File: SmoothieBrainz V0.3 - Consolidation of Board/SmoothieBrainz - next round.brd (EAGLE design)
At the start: 101 x 101 mm, 222 parts, among them IC1 LPC1769, IC5 LD117ADT33TR, Q1 BSL207SP, Q2 12MHz, SW1 SW_TACT_4P_B, SW3 SW_TACT_4P_B, T1 BC817, U3 USD-SOCKETUSD, X1 MSTBA2, X14 USBPTH, X2 GMSTBA2, X3 GMSTBA4, X4 1751248, X5 1751248, X6 1751248, X7 1751248

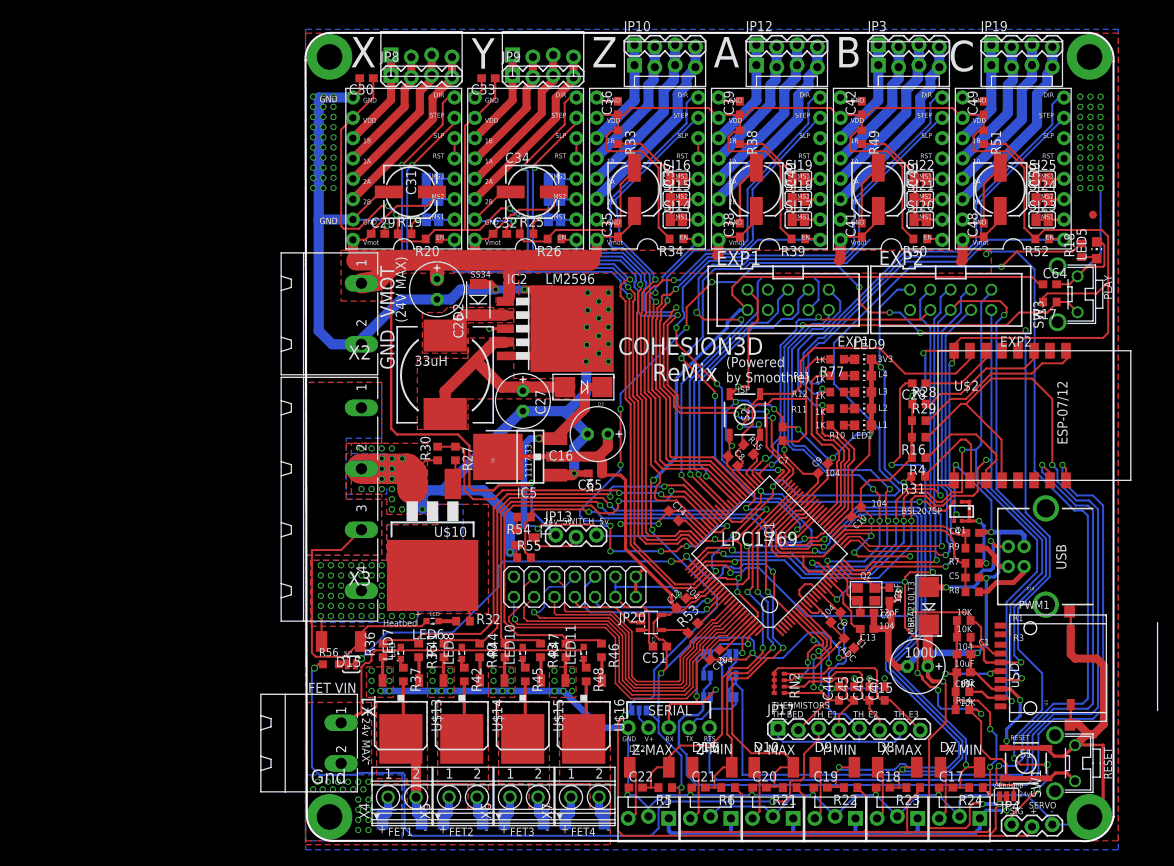
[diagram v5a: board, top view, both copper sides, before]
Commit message: motor 3 re-routed
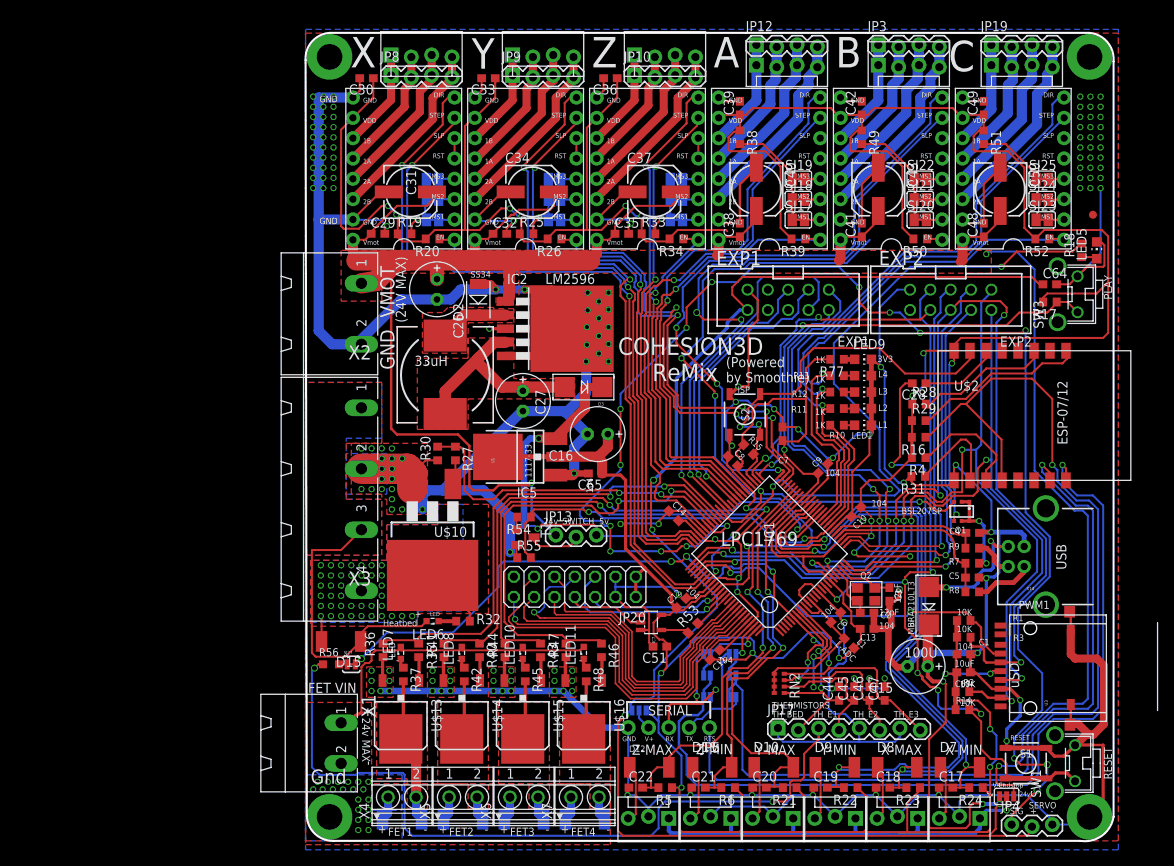
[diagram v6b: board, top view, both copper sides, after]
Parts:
- moved R33 12.7 mm to (42.9, 75.9), turned to 0 degrees
- moved C36 3.85 mm to (38.1, 95.3), turned to 180 degrees
- moved JP10 3.81 mm to (41.1, 95.6)
- moved C37 2.48 mm to (43.6, 81.1), turned to 0 degrees
- moved JP7 1.27 mm to (41.1, 98.1)
- moved C35 0.67 mm to (39.5, 75.9), turned to 0 degrees
- flipped SJ14 to the bottom, turned to 180 degrees
- flipped SJ15 to the bottom, turned to 180 degrees
- flipped SJ16 to the bottom, turned to 180 degrees
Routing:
- net 24V: track 256.6 -> 263.3 mm
- net N$24: track 13.9 -> 8.45 mm, vias 0 -> 1
- net DIR3: track 65.9 -> 61.5 mm, vias 1 -> 2
- net STP3: track 66.4 -> 62.5 mm, vias 1 -> 2
- net 3.3V: track 684.9 -> 687.1 mm, vias 23 -> 25
- net 2A3M: track 20.8 -> 19.5 mm
- net 1B3M: track 13.6 -> 12.4 mm
- net 1A3M: track 17.0 -> 15.7 mm
- net 2B3M: track 24.1 -> 22.9 mm
- net GND: track 776.5 -> 777.5 mm, vias 162 -> 163

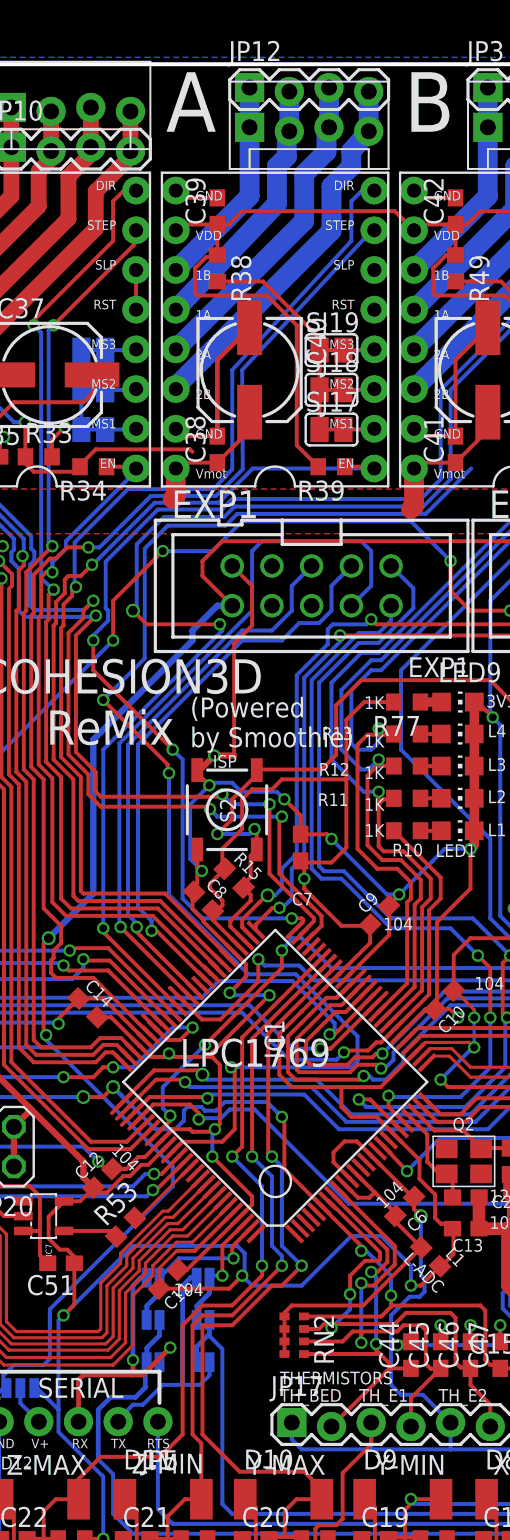
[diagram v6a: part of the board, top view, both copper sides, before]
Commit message: motor 4 wires
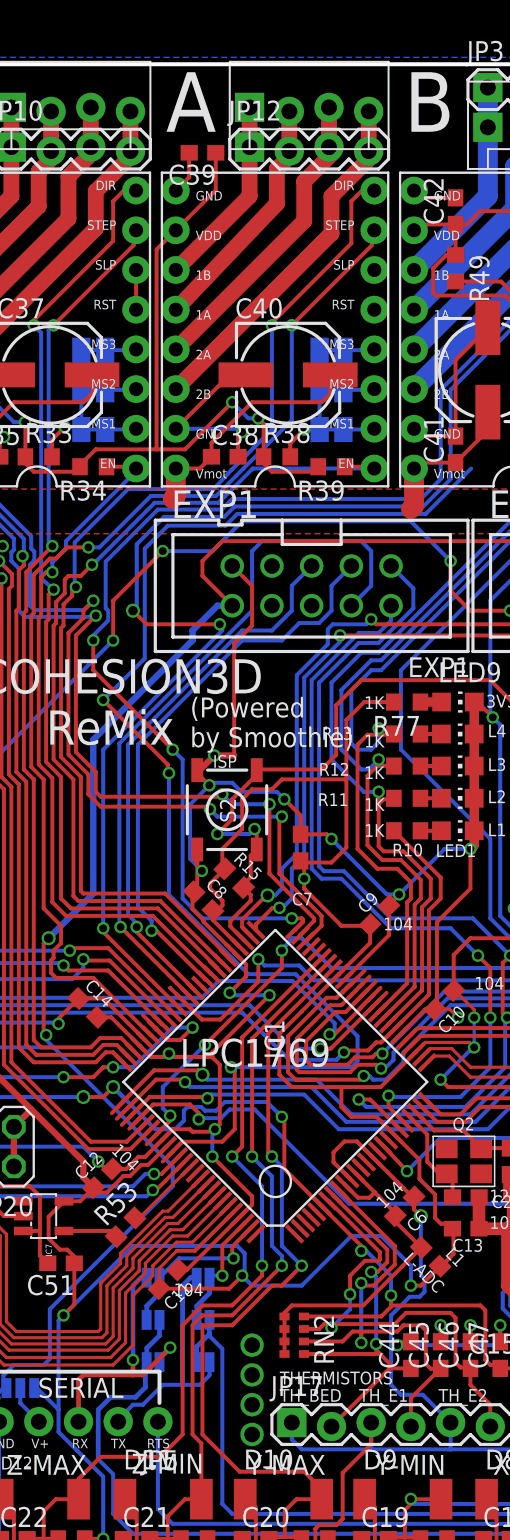
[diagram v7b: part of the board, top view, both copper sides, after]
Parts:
- moved R38 12.7 mm to (58.1, 75.9), turned to 0 degrees
- moved C39 3.85 mm to (53.3, 95.3), turned to 180 degrees
- moved JP12 3.81 mm to (56.4, 95.6)
- moved C40 2.48 mm to (58.8, 81.1), turned to 0 degrees
- moved JP11 1.27 mm to (56.4, 98.1)
- moved C38 0.67 mm to (54.8, 75.9), turned to 0 degrees
- flipped SJ17 to the bottom, turned to 180 degrees
- flipped SJ18 to the bottom, turned to 180 degrees
- flipped SJ19 to the bottom, turned to 180 degrees
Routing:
- net 24V: track 263.3 -> 269.7 mm
- net N$32: track 14.0 -> 8.41 mm, vias 0 -> 1
- net 3.3V: track 687.1 -> 682.4 mm, vias 25 -> 27
- net 1B$4M: track 13.6 -> 12.4 mm
- net 2B$4M: track 24.1 -> 22.9 mm
- net 2A$4M: track 20.8 -> 19.7 mm
- net 1A$4M: track 16.9 -> 15.7 mm
- net GND: track 777.5 -> 778.4 mm, vias 163 -> 164
- net STP4: track 69.5 -> 69.8 mm, vias 1 -> 2
- net DIR4: track 68.4 -> 68.6 mm, vias 1 -> 2

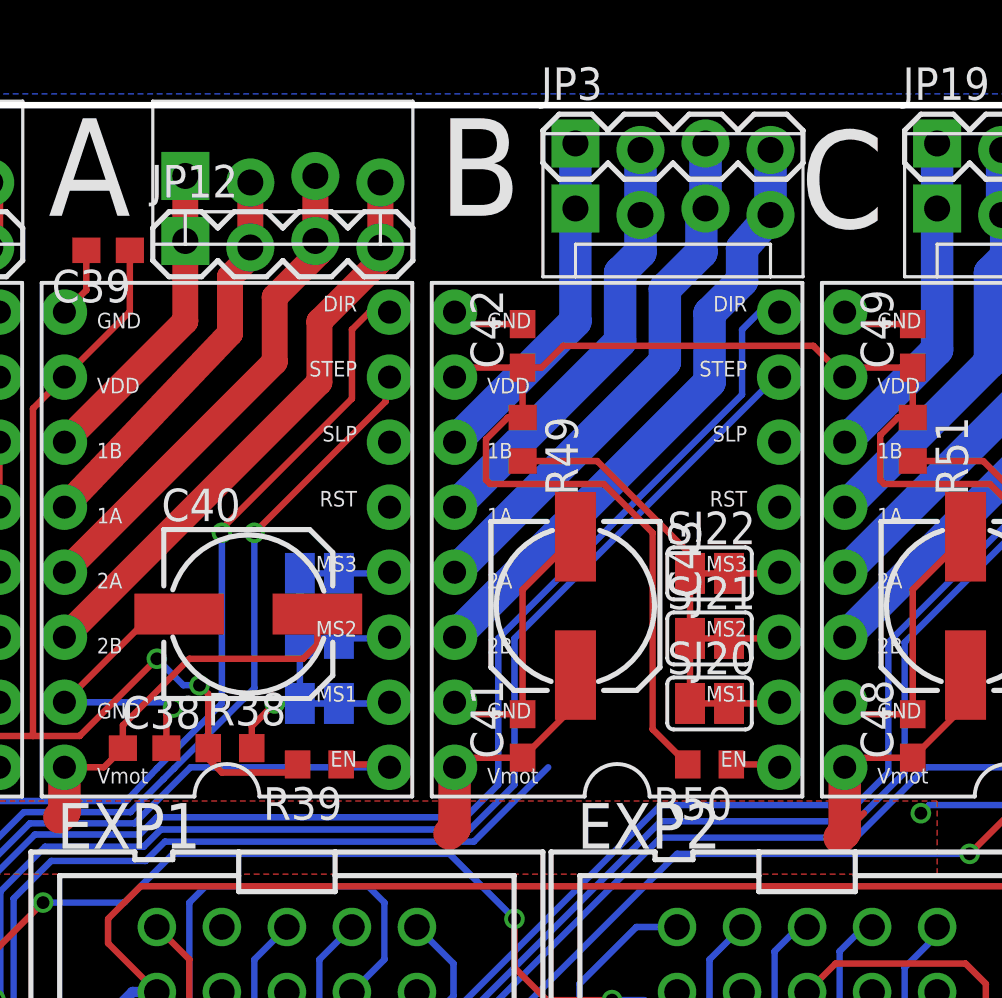
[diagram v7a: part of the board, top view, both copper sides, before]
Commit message: motor 5 wired
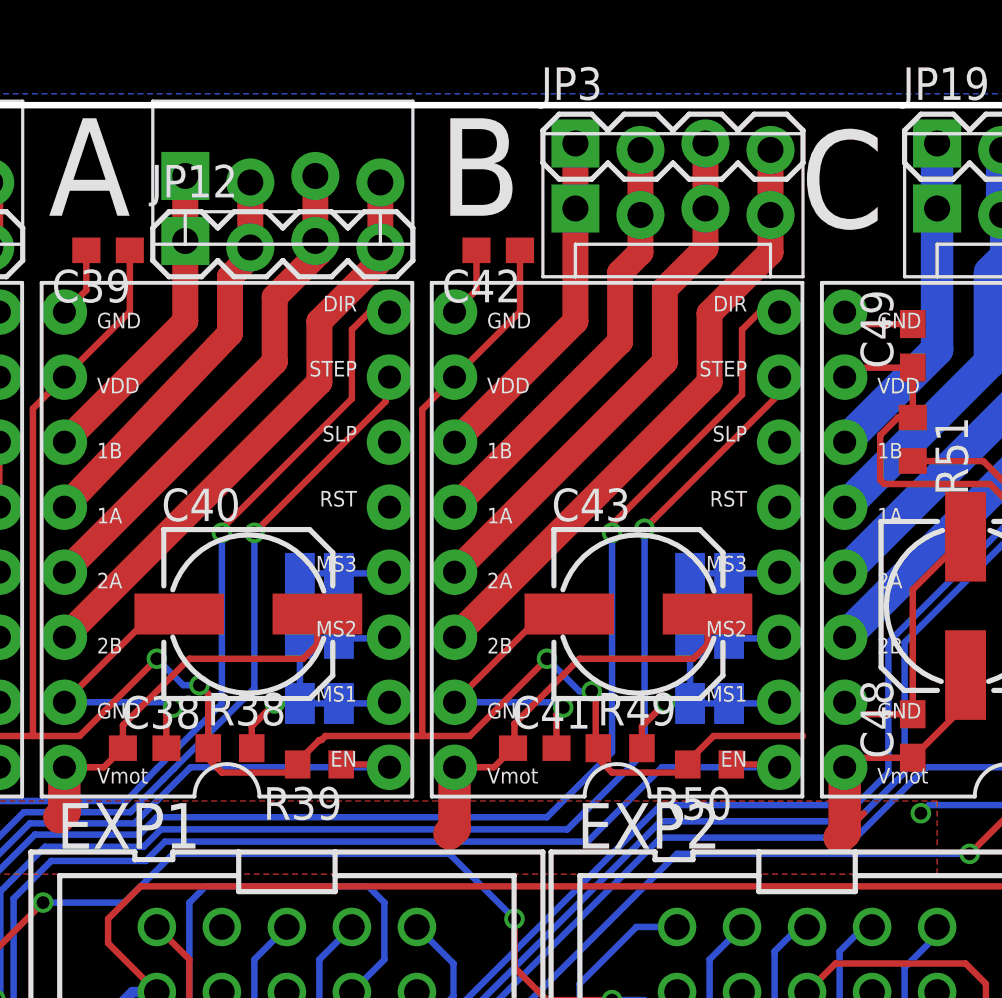
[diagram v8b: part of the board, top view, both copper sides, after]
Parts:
- moved R49 12.7 mm to (73.3, 75.9), turned to 0 degrees
- moved C42 3.85 mm to (68.6, 95.3), turned to 180 degrees
- moved C43 2.48 mm to (74.1, 81.1), turned to 0 degrees
- moved C41 0.67 mm to (70.0, 75.9), turned to 0 degrees
- flipped SJ20 to the bottom, turned to 180 degrees
- flipped SJ21 to the bottom, turned to 180 degrees
- flipped SJ22 to the bottom, turned to 180 degrees
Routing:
- net EN5: track 85.1 -> 94.2 mm
- net 3.3V: track 682.4 -> 689.9 mm, vias 27 -> 29
- net 24V: track 269.7 -> 276.3 mm
- net N$44: track 14.1 -> 8.18 mm, vias 0 -> 1
- net STP5: track 82.1 -> 84.2 mm, vias 3 -> 4
- net DIR5: track 80.6 -> 82.5 mm, vias 3 -> 4
- net GND: track 778.4 -> 779.6 mm, vias 164 -> 165
